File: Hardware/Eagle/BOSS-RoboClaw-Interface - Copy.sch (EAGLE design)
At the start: 9 parts, among them IC1 ISO7221ISO7221, J1 MOLEX 22112022, J2 MOLEX 22122034, J3 Amphenol 75869-130LF, J4 SAMTEC ESQ-105-44-G-S, J5 SAMTEC ESW-110-44-S-D, X1 Amphenol L77SDAH15SOL2RM8C309

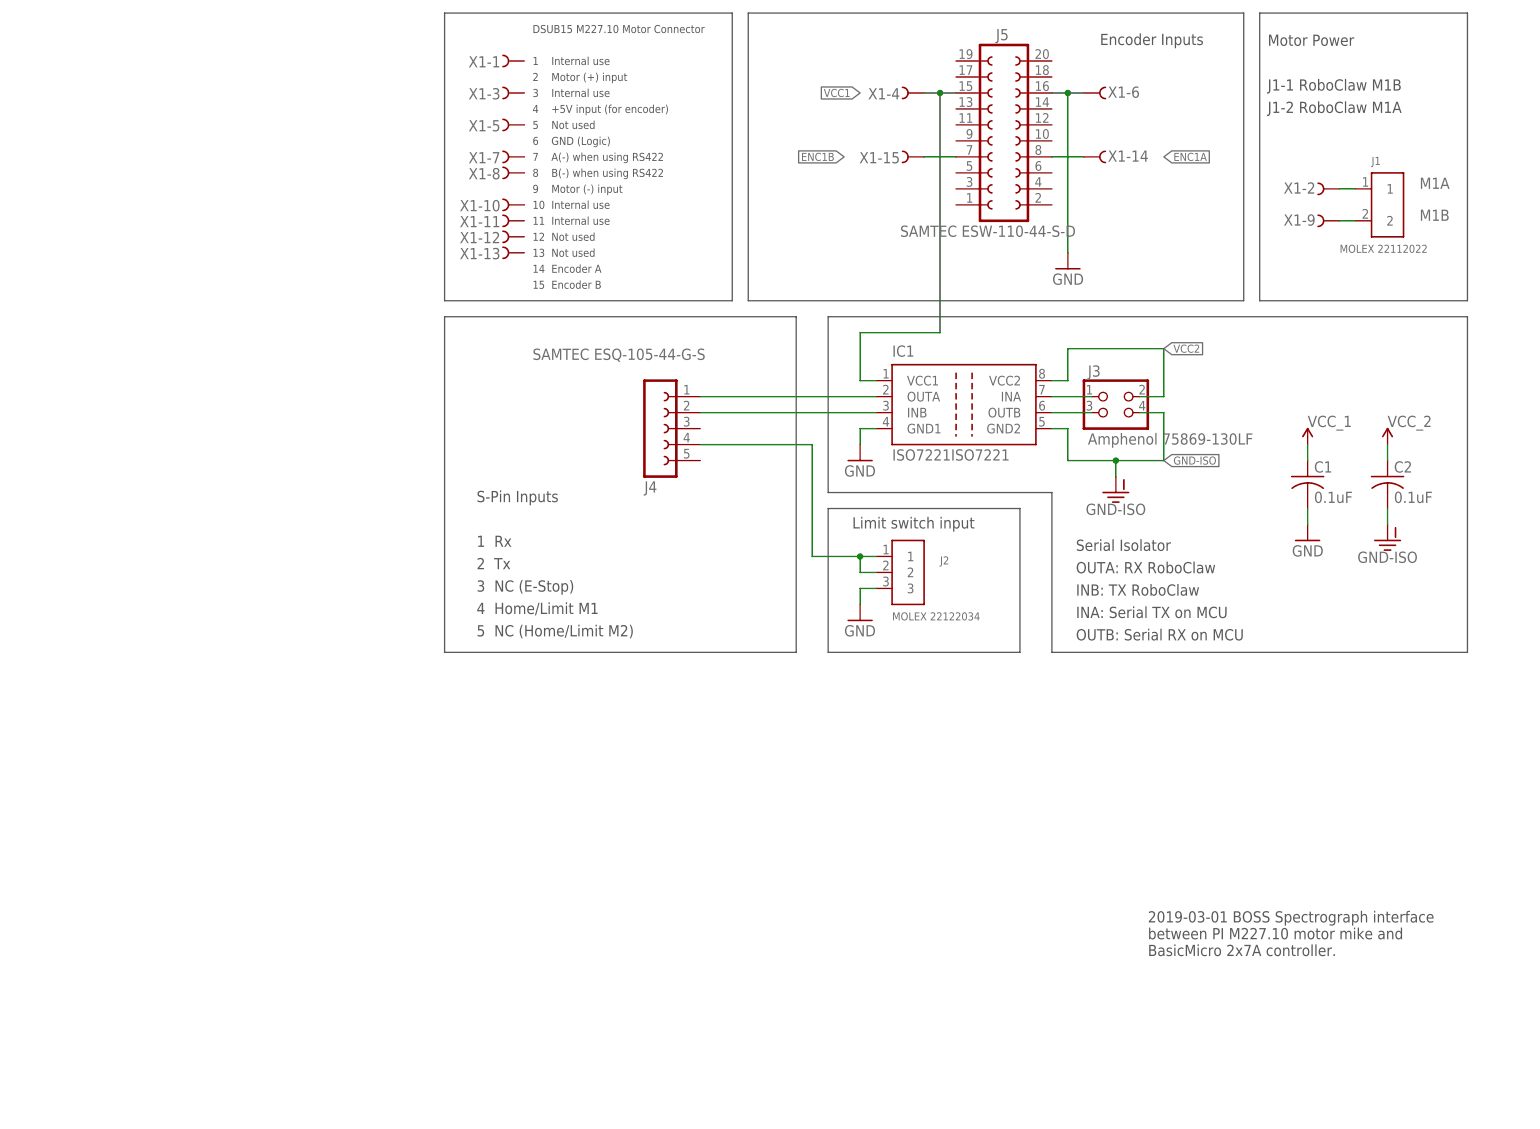
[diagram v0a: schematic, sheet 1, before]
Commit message: Changed connectors and board outline to be able to use existing screw connectors
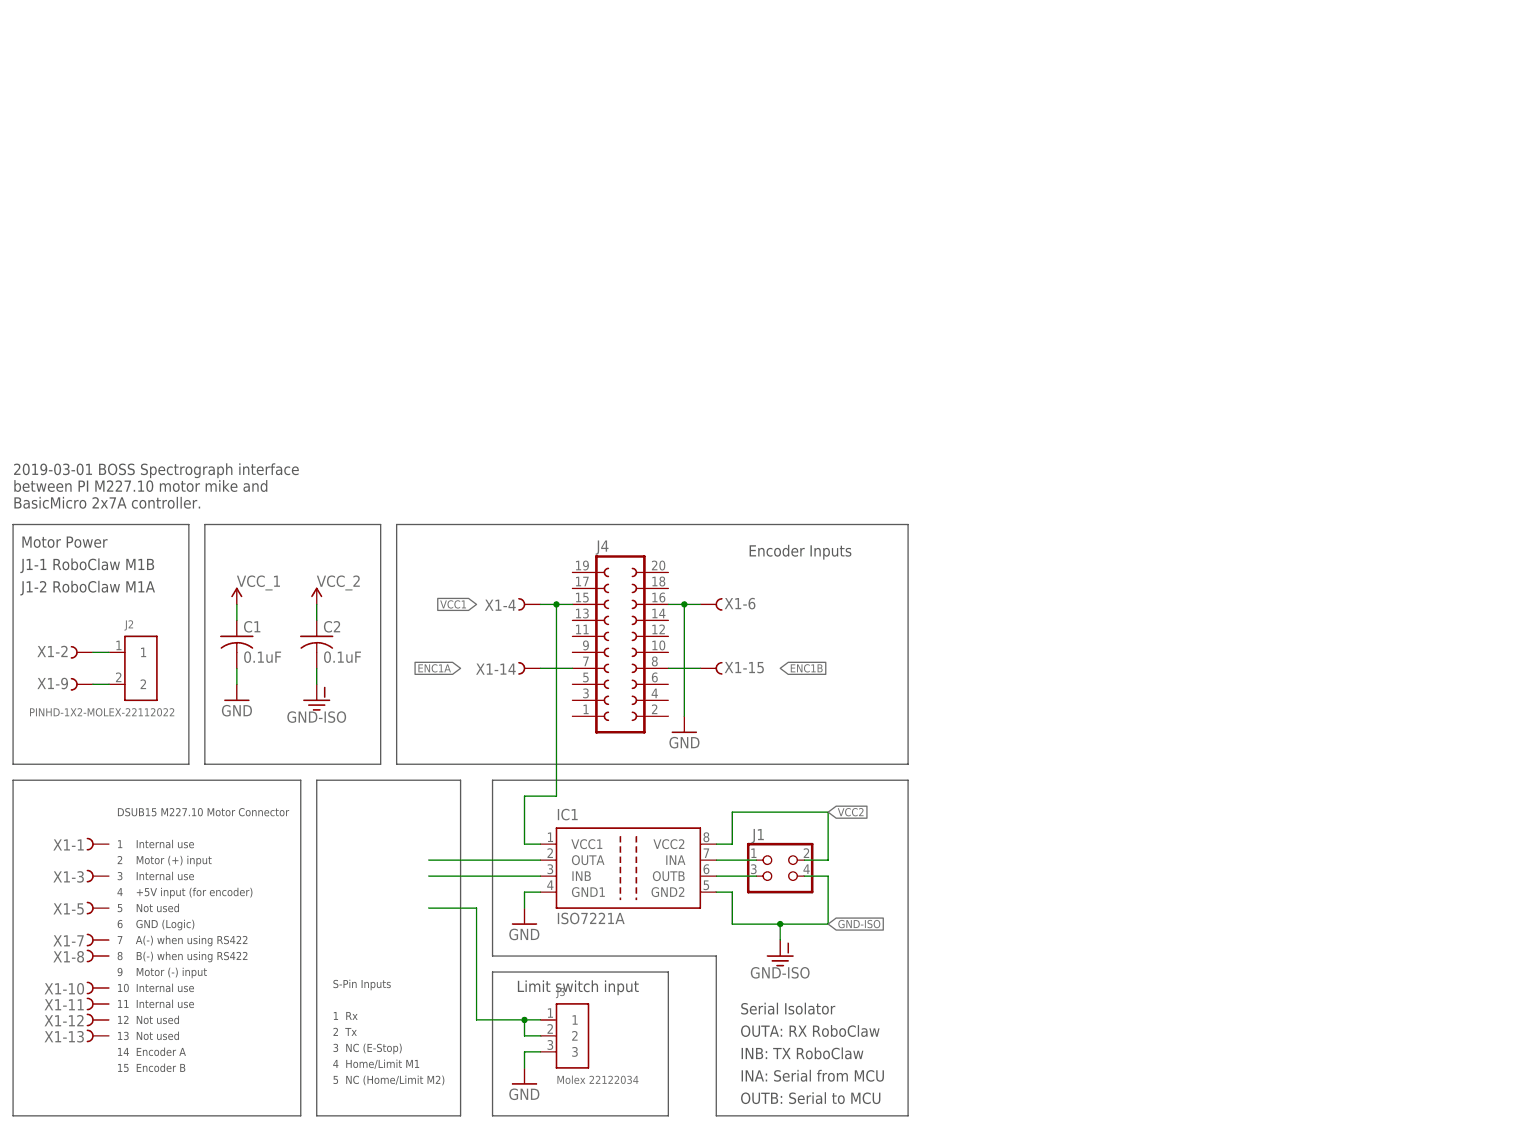
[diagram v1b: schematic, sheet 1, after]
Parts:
- removed J5: SAMTEC ESW-110-44-S-D, AUmlib:FE10-2SAMTEC-ESW-110-44-S-D
- IC1: value ISO7221ISO7221 -> ISO7221A; device AUmlib:ISO7221ISO7221 -> AUmlib:ISO7221A
- J1: value MOLEX 22112022 -> (none); device AUmlib:PINHD-1X2-MOLEX-22112022 -> AUmlib:PINHD-2X2AMP-75869-130LF
- J2: value MOLEX 22122034 -> PINHD-1X2-MOLEX-22112022; device AUmlib:PINHD-1X3RA-MOLEX-22122034 -> AUmlib:PINHD-1X2-MOLEX-22112022
- J3: value Amphenol 75869-130LF -> Molex 22122034; device AUmlib:PINHD-2X2AMP-75869-130LF -> AUmlib:PINHD-1X3RA-MOLEX-22122034
- J4: value SAMTEC ESQ-105-44-G-S -> (none); device AUmlib:FE05-1 -> AUmlib:FE10-2SAMTEC-ESW-110-44-S-D
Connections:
- removed net LIMIT: J2.1, J2.2, J4.4
- removed net RXMCU: IC1.OUTB, J3.3
- removed net TXMCU: IC1.INA, J3.1
- new net LIMIT/HOME: J3.1, J3.2
- new net N$1: IC1.INA, J1.1
- new net N$2: IC1.OUTB, J1.3
- net ENC1A: now also J4.7; no longer J5.8
- net ENC1B: now also J4.8; no longer J5.7
- net GND: now also J3.3, J4.16; no longer J2.3, J5.16
- net GND-ISO: now also J1.4; no longer J3.4
- net M1A: now also J2.2, X1-9.F; no longer J1.1, X1-2.F
- net M1B: now also J2.1, X1-2.F; no longer J1.2, X1-9.F
- net RX: no longer J4.1
- net TX: no longer J4.2
- net VCC1: now also J4.15; no longer J5.15
- net VCC2: now also J1.2; no longer J3.2
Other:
- note added: "Serial Isolator OUTA: RX RoboClaw INB: TX RoboClaw INA: Serial from MCU OUTB: Serial to MCU"
- note removed: "Serial Isolator OUTA: RX RoboClaw INB: TX RoboClaw INA: Serial TX on MCU OUTB: Serial RX on MCU"
- moved on the sheet: C1, C2, IC1, X1-1, X1-10, X1-11, X1-12, X1-13, X1-14, X1-15, X1-2, X1-3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
